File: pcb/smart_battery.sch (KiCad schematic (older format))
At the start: 32 parts, among them J1 feather long, J10 feather short, J11 Conn_01x05_RTC, J12 Conn_HtrTh, J13 Conn_BattTh, J2 feather short, J3 feather long, J4 feather short, J5 feather long, J6 feather short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

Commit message: Placed resistor and capacitor pads
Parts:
- C1, C2, C3: footprint (none) -> Capacitor_SMD:C_0805_2012Metric
- R1, R2, R3, R4, R5: footprint (none) -> Resistor_SMD:R_0805_2012Metric
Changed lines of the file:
@@
 EESchema Schematic File Version 4
-EELAYER 30 0
+LIBS:smart_battery-cache
+EELAYER 26 0
 EELAYER END
 $Descr USLetter 11000 8500
@@
 F 0 "R1" H 5420 2346 50  0000 L CNN
 F 1 "R2k" H 5420 2255 50  0000 L CNN
-F 2 "" V 5280 2300 50  0001 C CNN
+F 2 "Resistor_SMD:R_0805_2012Metric" V 5280 2300 50  0001 C CNN
 F 3 "~" H 5350 2300 50  0001 C CNN
 	1    5350 2300
@@
 F 0 "R2" H 5670 2346 50  0000 L CNN
 F 1 "R2k" H 5670 2255 50  0000 L CNN
-F 2 "" V 5530 2300 50  0001 C CNN
+F 2 "Resistor_SMD:R_0805_2012Metric" V 5530 2300 50  0001 C CNN
 F 3 "~" H 5600 2300 50  0001 C CNN
 	1    5600 2300
@@
 F 0 "R3" H 1570 1896 50  0000 L CNN
 F 1 "R10k" H 1570 1805 50  0000 L CNN
-F 2 "" V 1430 1850 50  0001 C CNN
+F 2 "Resistor_SMD:R_0805_2012Metric" V 1430 1850 50  0001 C CNN
 F 3 "~" H 1500 1850 50  0001 C CNN
 	1    1500 1850
@@
 F 0 "R4" H 1870 1896 50  0000 L CNN
 F 1 "R10k" H 1870 1805 50  0000 L CNN
-F 2 "" V 1730 1850 50  0001 C CNN
+F 2 "Resistor_SMD:R_0805_2012Metric" V 1730 1850 50  0001 C CNN
 F 3 "~" H 1800 1850 50  0001 C CNN
 	1    1800 1850
@@
 F 0 "C2" H 9665 3646 50  0000 L CNN
 F 1 "C10uF" H 9665 3555 50  0000 L CNN
-F 2 "" H 9588 3450 50  0001 C CNN
+F 2 "Capacitor_SMD:C_0805_2012Metric" H 9588 3450 50  0001 C CNN
 F 3 "~" H 9550 3600 50  0001 C CNN
 	1    9550 3600
@@
 F 0 "C3" H 10015 3646 50  0000 L CNN
 F 1 "C1uF" H 10015 3555 50  0000 L CNN
-F 2 "" H 9938 3450 50  0001 C CNN
+F 2 "Capacitor_SMD:C_0805_2012Metric" H 9938 3450 50  0001 C CNN
 F 3 "~" H 9900 3600 50  0001 C CNN
 	1    9900 3600
@@
 F 0 "R5" V 8404 3550 50  0000 C CNN
 F 1 "100K" V 8495 3550 50  0000 C CNN
-F 2 "" H 8600 3550 50  0001 C CNN
+F 2 "Resistor_SMD:R_0805_2012Metric" H 8600 3550 50  0001 C CNN
 F 3 "~" H 8600 3550 50  0001 C CNN
 	1    8600 3550
@@
 F 0 "C1" H 8615 3746 50  0000 L CNN
 F 1 "C10uF" H 8615 3655 50  0000 L CNN
-F 2 "" H 8538 3550 50  0001 C CNN
+F 2 "Capacitor_SMD:C_0805_2012Metric" H 8538 3550 50  0001 C CNN
 F 3 "~" H 8500 3700 50  0001 C CNN
 	1    8500 3700

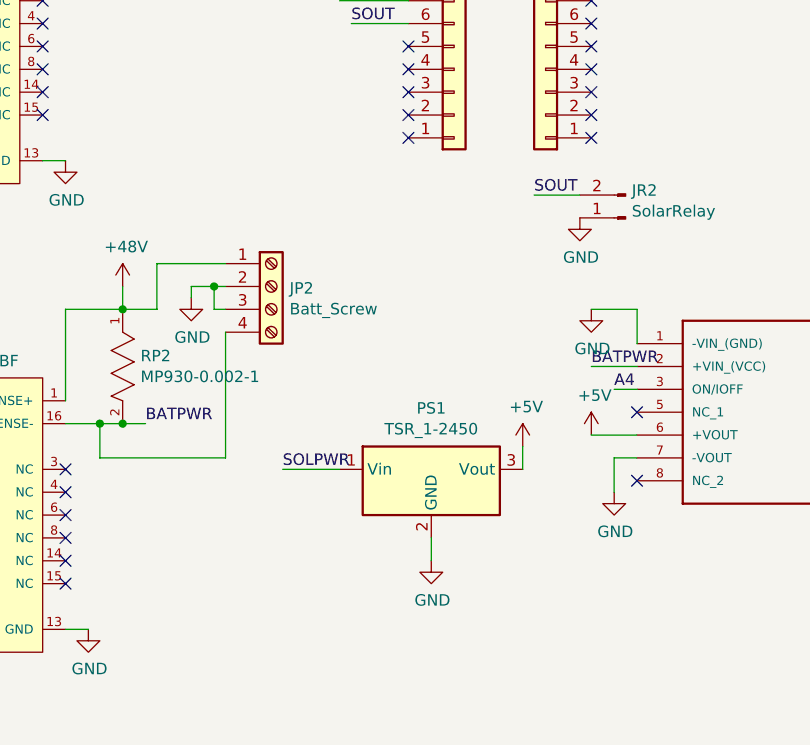
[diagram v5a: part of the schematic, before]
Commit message: Added switches to power battery module from large battery
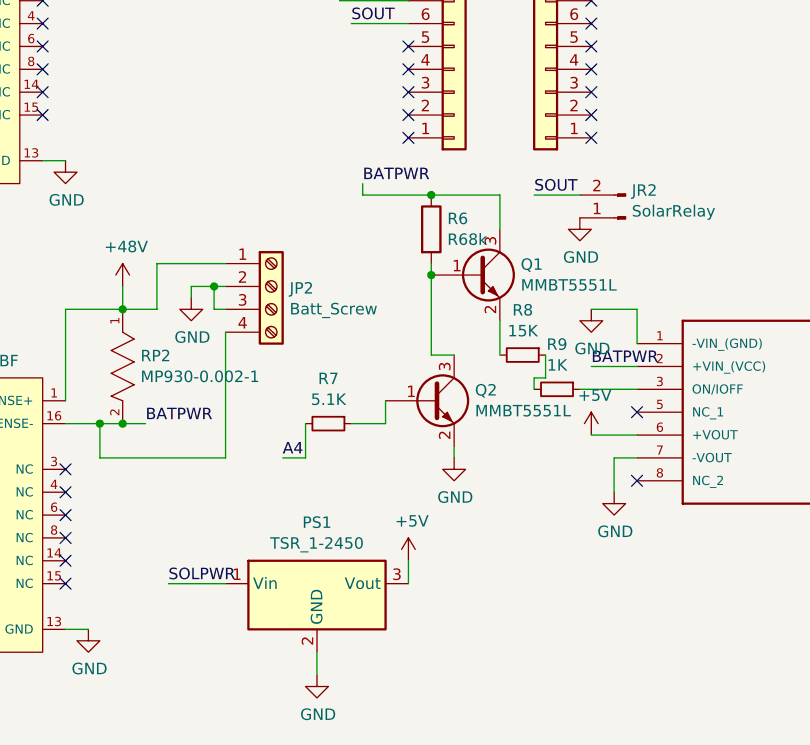
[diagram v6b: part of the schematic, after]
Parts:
- added Q1, Q2: MMBT5551L, Package_TO_SOT_SMD:SOT-23, symbol Transistor_BJT:MMBT5551L
- added R6: R68k, Resistor_SMD:R_0805_2012Metric, symbol Device:R
- added R7: 5.1K, Resistor_SMD:R_0805_2012Metric, symbol Device:R_Small
- added R8: 15K, Resistor_SMD:R_0805_2012Metric, symbol Device:R_Small
- added R9: 1K, Resistor_SMD:R_0805_2012Metric, symbol Device:R_Small
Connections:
- net A4: now also R7.2; no longer PS2.3 (ON/IOFF)
- net BATPWR: now also Q1.3 (C), R6.1
- net GND: now also Q2.2 (E)
- new net: PS2.3 (ON/IOFF), R9.1
- new net: Q1.1 (B), Q2.3 (C), R6.2
- new net: Q1.2 (E), R8.2
- new net: Q2.1 (B), R7.1
- new net: R8.1, R9.2
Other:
- moved on the sheet: PS1
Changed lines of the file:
@@
 L Regulator_Switching:TSR_1-2450 PS1
 U 1 1 601BDF5C
-P 4100 6650
-F 0 "PS1" H 4100 7017 50  0000 C CNN
-F 1 "TSR_1-2450" H 4100 6926 50  0000 C CNN
-F 2 "Converter_DCDC:Converter_DCDC_TRACO_TSR-1_THT" H 4100 6500 50  0001 L CIN
-F 3 "http://www.tracopower.com/products/tsr1.pdf" H 4100 6650 50  0001 C CNN
-	1    4100 6650
+P 3600 7150
+F 0 "PS1" H 3600 7517 50  0000 C CNN
+F 1 "TSR_1-2450" H 3600 7426 50  0000 C CNN
+F 2 "Converter_DCDC:Converter_DCDC_TRACO_TSR-1_THT" H 3600 7000 50  0001 L CIN
+F 3 "http://www.tracopower.com/products/tsr1.pdf" H 3600 7150 50  0001 C CNN
+	1    3600 7150
 	1    0    0    -1
 $EndComp
@@
 L power:GND #PWR018
 U 1 1 601C73D5
-P 4100 6950
-F 0 "#PWR018" H 4100 6700 50  0001 C CNN
-F 1 "GND" H 4105 6777 50  0000 C CNN
-F 2 "" H 4100 6950 50  0001 C CNN
-F 3 "" H 4100 6950 50  0001 C CNN
-	1    4100 6950
-	1    0    0    -1
-$EndComp
-Wire Wire Line
-	4100 6950 4100 6850
+P 3600 7450
+F 0 "#PWR018" H 3600 7200 50  0001 C CNN
+F 1 "GND" H 3605 7277 50  0000 C CNN
+F 2 "" H 3600 7450 50  0001 C CNN
+F 3 "" H 3600 7450 50  0001 C CNN
+	1    3600 7450
+	1    0    0    -1
+$EndComp
+Wire Wire Line
+	3600 7450 3600 7350
 $Comp
 L power:+5V #PWR019
 U 1 1 601CCD37
-P 4500 6450
-F 0 "#PWR019" H 4500 6300 50  0001 C CNN
-F 1 "+5V" H 4515 6623 50  0000 C CNN
-F 2 "" H 4500 6450 50  0001 C CNN
-F 3 "" H 4500 6450 50  0001 C CNN
-	1    4500 6450
-	1    0    0    -1
-$EndComp
-Wire Wire Line
-	4500 6450 4500 6550
+P 4000 6950
+F 0 "#PWR019" H 4000 6800 50  0001 C CNN
+F 1 "+5V" H 4015 7123 50  0000 C CNN
+F 2 "" H 4000 6950 50  0001 C CNN
+F 3 "" H 4000 6950 50  0001 C CNN
+	1    4000 6950
+	1    0    0    -1
+$EndComp
+Wire Wire Line
+	4000 6950 4000 7050
 $Comp
 L TEC_2-2411:TEC_2-2411 PS2
@@
 Wire Wire Line
 	4900 6500 5000 6500
-Wire Wire Line
-	4800 5850 5000 5850
-Wire Wire Line
-	5000 5850 5000 6000
-Text Label 4900 6200 0    50   ~ 0
+Text Label 3450 6500 0    50   ~ 0
 A4
-Wire Wire Line
-	4900 6200 5000 6200
 Wire Wire Line
 	2400 3800 2650 3800
@@
 	2750 4300 2650 4300
 Connection ~ 2650 4300
-Text Label 3450 6550 0    50   ~ 0
+Text Label 2950 7050 0    50   ~ 0
 SOLPWR
 Wire Wire Line
-	3450 6550 3700 6550
+	2950 7050 3200 7050
 $Comp
 L Connector:Screw_Terminal_01x04 JP2
@@
 Wire Wire Line
 	3200 3850 3250 3850
+$Comp
+L Transistor_BJT:MMBT5551L Q1
+U 1 1 601F74BC
+P 4300 5700
+F 0 "Q1" H 4491 5746 50  0000 L CNN
+F 1 "MMBT5551L" H 4491 5655 50  0000 L CNN
+F 2 "Package_TO_SOT_SMD:SOT-23" H 4500 5625 50  0001 L CIN
+F 3 "www.onsemi.com/pub/Collateral/MMBT5550LT1-D.PDF" H 4300 5700 50  0001 L CNN
+	1    4300 5700
+	1    0    0    -1
+$EndComp
+$Comp
+L Transistor_BJT:MMBT5551L Q2
+U 1 1 601F767C
+P 4100 6250
+F 0 "Q2" H 4291 6296 50  0000 L CNN
+F 1 "MMBT5551L" H 4291 6205 50  0000 L CNN
+F 2 "Package_TO_SOT_SMD:SOT-23" H 4300 6175 50  0001 L CIN
+F 3 "www.onsemi.com/pub/Collateral/MMBT5550LT1-D.PDF" H 4100 6250 50  0001 L CNN
+	1    4100 6250
+	1    0    0    -1
+$EndComp
+Wire Wire Line
+	5000 5850 5000 6000
+Wire Wire Line
+	4800 5850 5000 5850
+Text Label 3800 5300 0    50   ~ 0
+BATPWR
+Wire Wire Line
+	3800 5300 3800 5350
+Wire Wire Line
+	3800 5350 4100 5350
+$Comp
+L Device:R R6
+U 1 1 602110C3
+P 4100 5500
+F 0 "R6" H 4170 5546 50  0000 L CNN
+F 1 "R68k" H 4170 5455 50  0000 L CNN
+F 2 "Resistor_SMD:R_0805_2012Metric" V 4030 5500 50  0001 C CNN
+F 3 "~" H 4100 5500 50  0001 C CNN
+	1    4100 5500
+	1    0    0    -1
+$EndComp
+Wire Wire Line
+	4100 5650 4100 5700
+Wire Wire Line
+	4100 5700 4100 6050
+Connection ~ 4100 5700
+Wire Wire Line
+	4100 6050 4200 6050
+$Comp
+L power:GND #PWR?
+U 1 1 6024E55B
+P 4200 6500
+F 0 "#PWR?" H 4200 6250 50  0001 C CNN
+F 1 "GND" H 4205 6327 50  0000 C CNN
+F 2 "" H 4200 6500 50  0001 C CNN
+F 3 "" H 4200 6500 50  0001 C CNN
+	1    4200 6500
+	1    0    0    -1
+$EndComp
+Wire Wire Line
+	4200 6450 4200 6500
+$Comp
+L Device:R_Small R8
+U 1 1 602A73D7
+P 4500 6050
+F 0 "R8" V 4304 6050 50  0000 C CNN
+F 1 "15K" V 4395 6050 50  0000 C CNN
+F 2 "Resistor_SMD:R_0805_2012Metric" H 4500 6050 50  0001 C CNN
+F 3 "~" H 4500 6050 50  0001 C CNN
+	1    4500 6050
+	0    1    1    0
+$EndComp
+$Comp
+L Device:R_Small R7
+U 1 1 602A7634
+P 3650 6350
+F 0 "R7" V 3454 6350 50  0000 C CNN
+F 1 "5.1K" V 3545 6350 50  0000 C CNN
+F 2 "Resistor_SMD:R_0805_2012Metric" H 3650 6350 50  0001 C CNN
+F 3 "~" H 3650 6350 50  0001 C CNN
+	1    3650 6350
+	0    1    1    0
+$EndComp
+Wire Wire Line
+	3450 6500 3550 6500
+Wire Wire Line
+	3550 6500 3550 6350
+Wire Wire Line
+	3750 6350 3900 6350
+Wire Wire Line
+	3900 6350 3900 6250
+$Comp
+L Device:R_Small R9
+U 1 1 602B9960
+P 4650 6200
+F 0 "R9" V 4454 6200 50  0000 C CNN
+F 1 "1K" V 4545 6200 50  0000 C CNN
+F 2 "Resistor_SMD:R_0805_2012Metric" H 4650 6200 50  0001 C CNN
+F 3 "~" H 4650 6200 50  0001 C CNN
+	1    4650 6200
+	0    1    1    0
+$EndComp
+Wire Wire Line
+	4400 5900 4400 6050
+Wire Wire Line
+	4600 6050 4600 6150
+Wire Wire Line
+	4600 6150 4550 6150
+Wire Wire Line
+	4550 6150 4550 6200
+Wire Wire Line
+	4750 6200 5000 6200
+Wire Wire Line
+	4100 5350 4400 5350
+Wire Wire Line
+	4400 5350 4400 5500
+Connection ~ 4100 5350
 $EndSCHEMATC

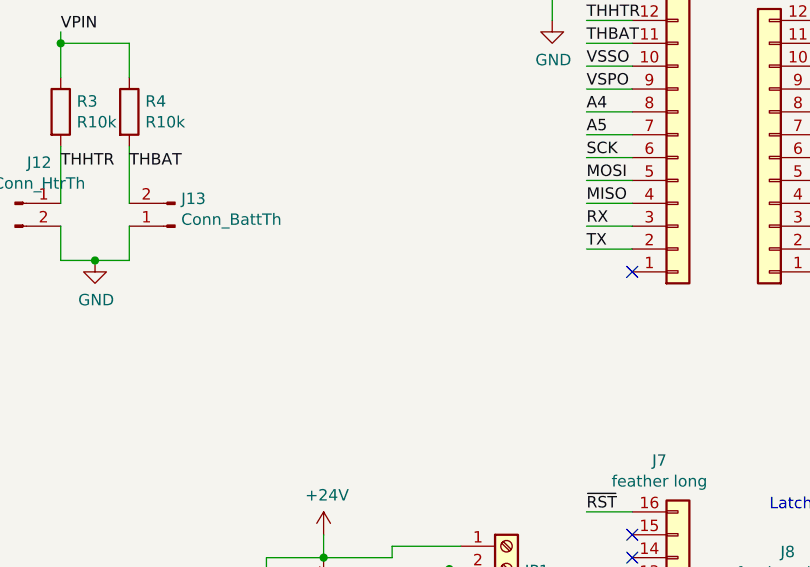
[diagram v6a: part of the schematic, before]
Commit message: Added rockblock modem connection
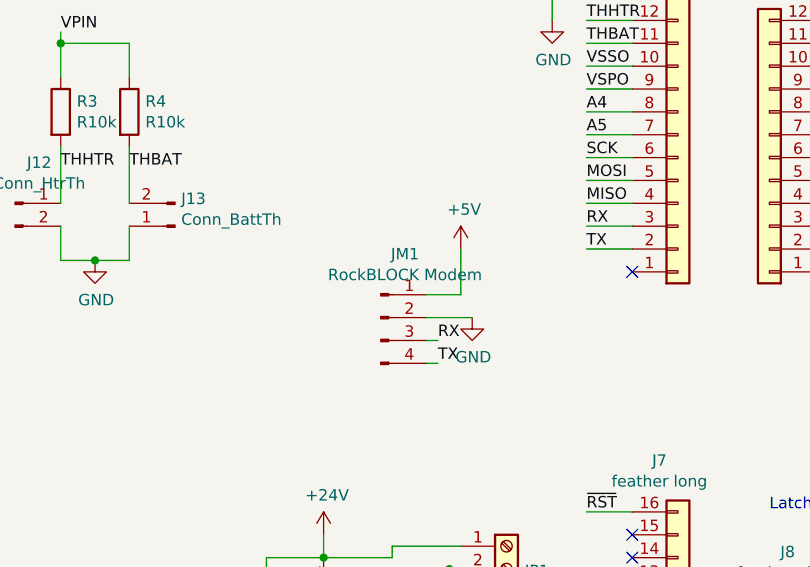
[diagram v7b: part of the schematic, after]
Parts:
- added JM1: RockBLOCK Modem, symbol Connector:Conn_01x04_Male
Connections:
- net +5V: now also JM1.1 (Pin_1)
- net GND: now also JM1.2 (Pin_2)
- net RX: now also JM1.3 (Pin_3)
- net TX: now also JM1.4 (Pin_4)
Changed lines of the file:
@@
 	4400 5350 4400 5500
 Connection ~ 4100 5350
+$Comp
+L Connector:Conn_01x04_Male JM1
+U 1 1 601F67BE
+P 2900 2750
+F 0 "JM1" H 3006 3028 50  0000 C CNN
+F 1 "RockBLOCK Modem" H 3006 2937 50  0000 C CNN
+F 2 "" H 2900 2750 50  0001 C CNN
+F 3 "~" H 2900 2750 50  0001 C CNN
+	1    2900 2750
+	1    0    0    -1
+$EndComp
+$Comp
+L power:+5V #PWR?
+U 1 1 601F6B4D
+P 3250 2450
+F 0 "#PWR?" H 3250 2300 50  0001 C CNN
+F 1 "+5V" H 3265 2623 50  0000 C CNN
+F 2 "" H 3250 2450 50  0001 C CNN
+F 3 "" H 3250 2450 50  0001 C CNN
+	1    3250 2450
+	1    0    0    -1
+$EndComp
+Wire Wire Line
+	3100 2650 3250 2650
+Wire Wire Line
+	3250 2650 3250 2450
+$Comp
+L power:GND #PWR?
+U 1 1 602008F6
+P 3300 2750
+F 0 "#PWR?" H 3300 2500 50  0001 C CNN
+F 1 "GND" H 3305 2577 50  0000 C CNN
+F 2 "" H 3300 2750 50  0001 C CNN
+F 3 "" H 3300 2750 50  0001 C CNN
+	1    3300 2750
+	1    0    0    -1
+$EndComp
+Wire Wire Line
+	3100 2750 3300 2750
+Text Label 3150 2850 0    50   ~ 0
+RX
+Text Label 3150 2950 0    50   ~ 0
+TX
+Wire Wire Line
+	3100 2850 3150 2850
+Wire Wire Line
+	3100 2950 3150 2950
 $EndSCHEMATC
